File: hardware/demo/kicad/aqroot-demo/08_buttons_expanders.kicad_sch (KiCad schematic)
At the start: 34 parts, among them SW2 UP, SW3 DOWN, SW4 LEFT, SW5 RIGHT, SW6 A_SELECT, SW7 B_BACK, U2 PCAL9535APW, U23 PCAL9535APW, U3 PCAL9535APW

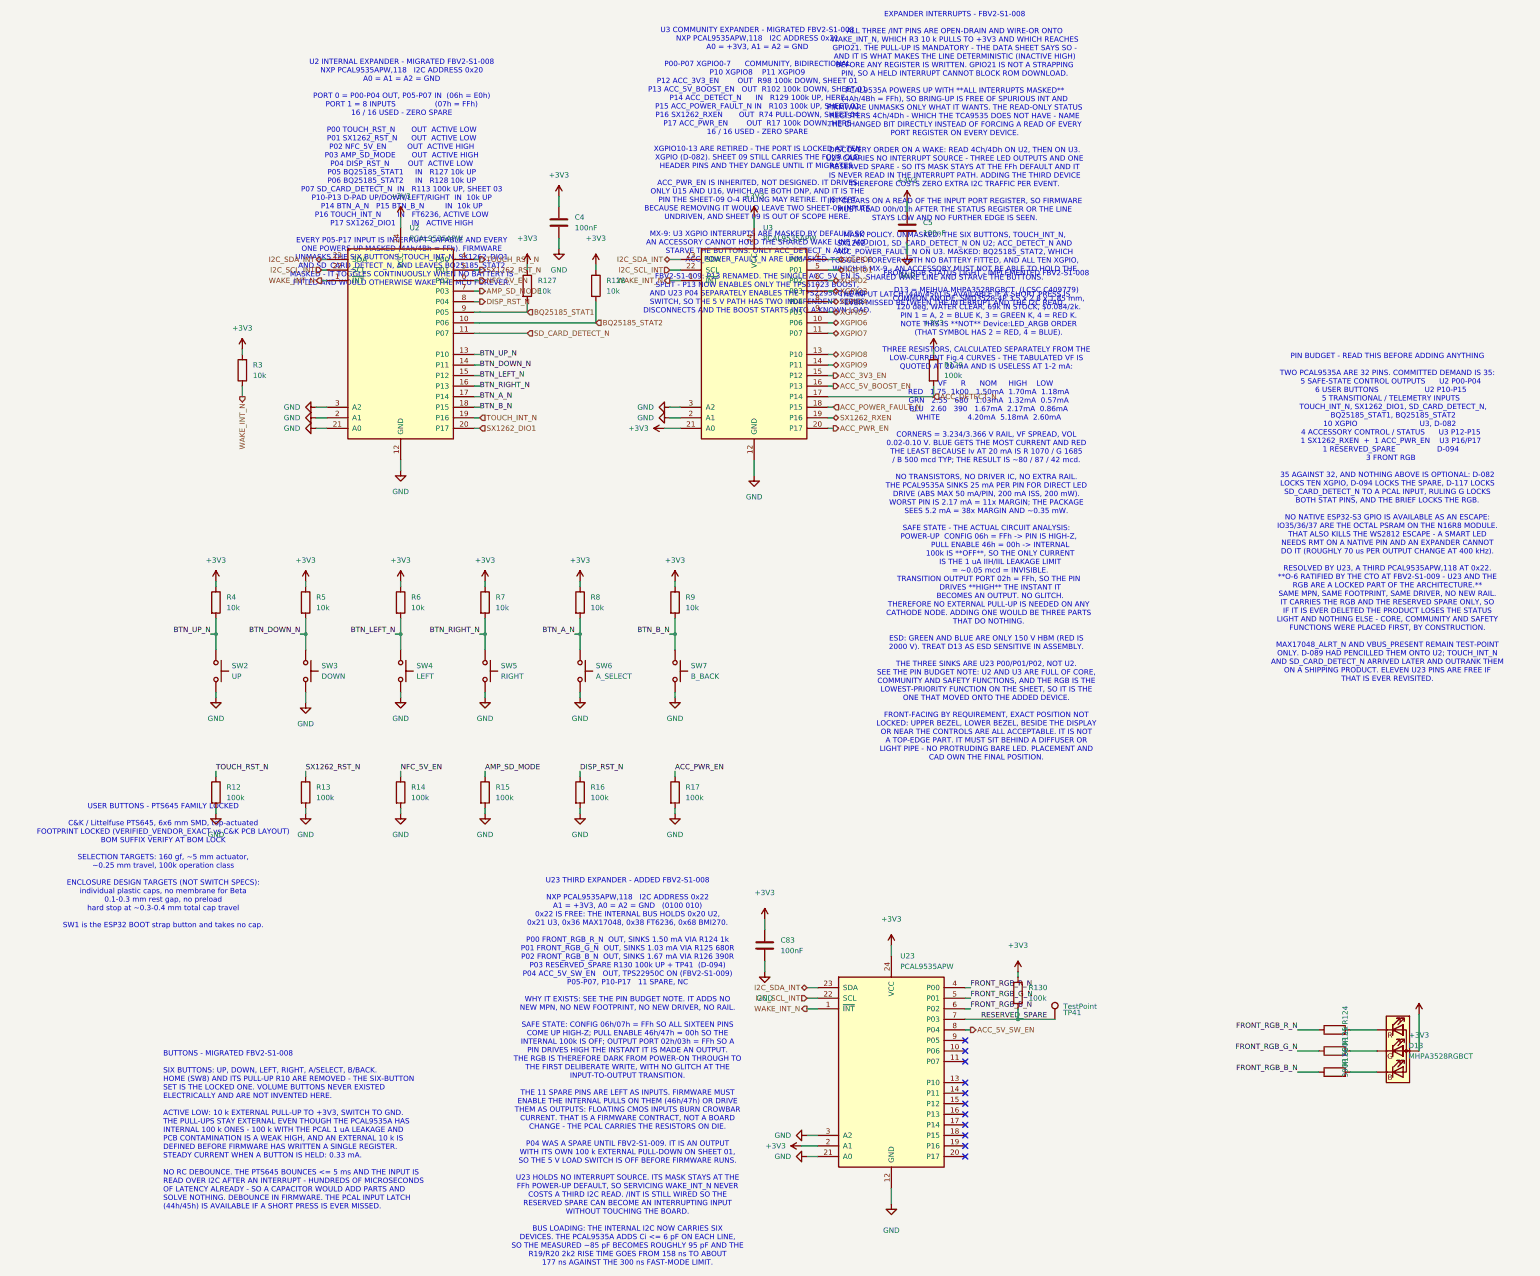
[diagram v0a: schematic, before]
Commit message: demo: apply schematic simplification ECO
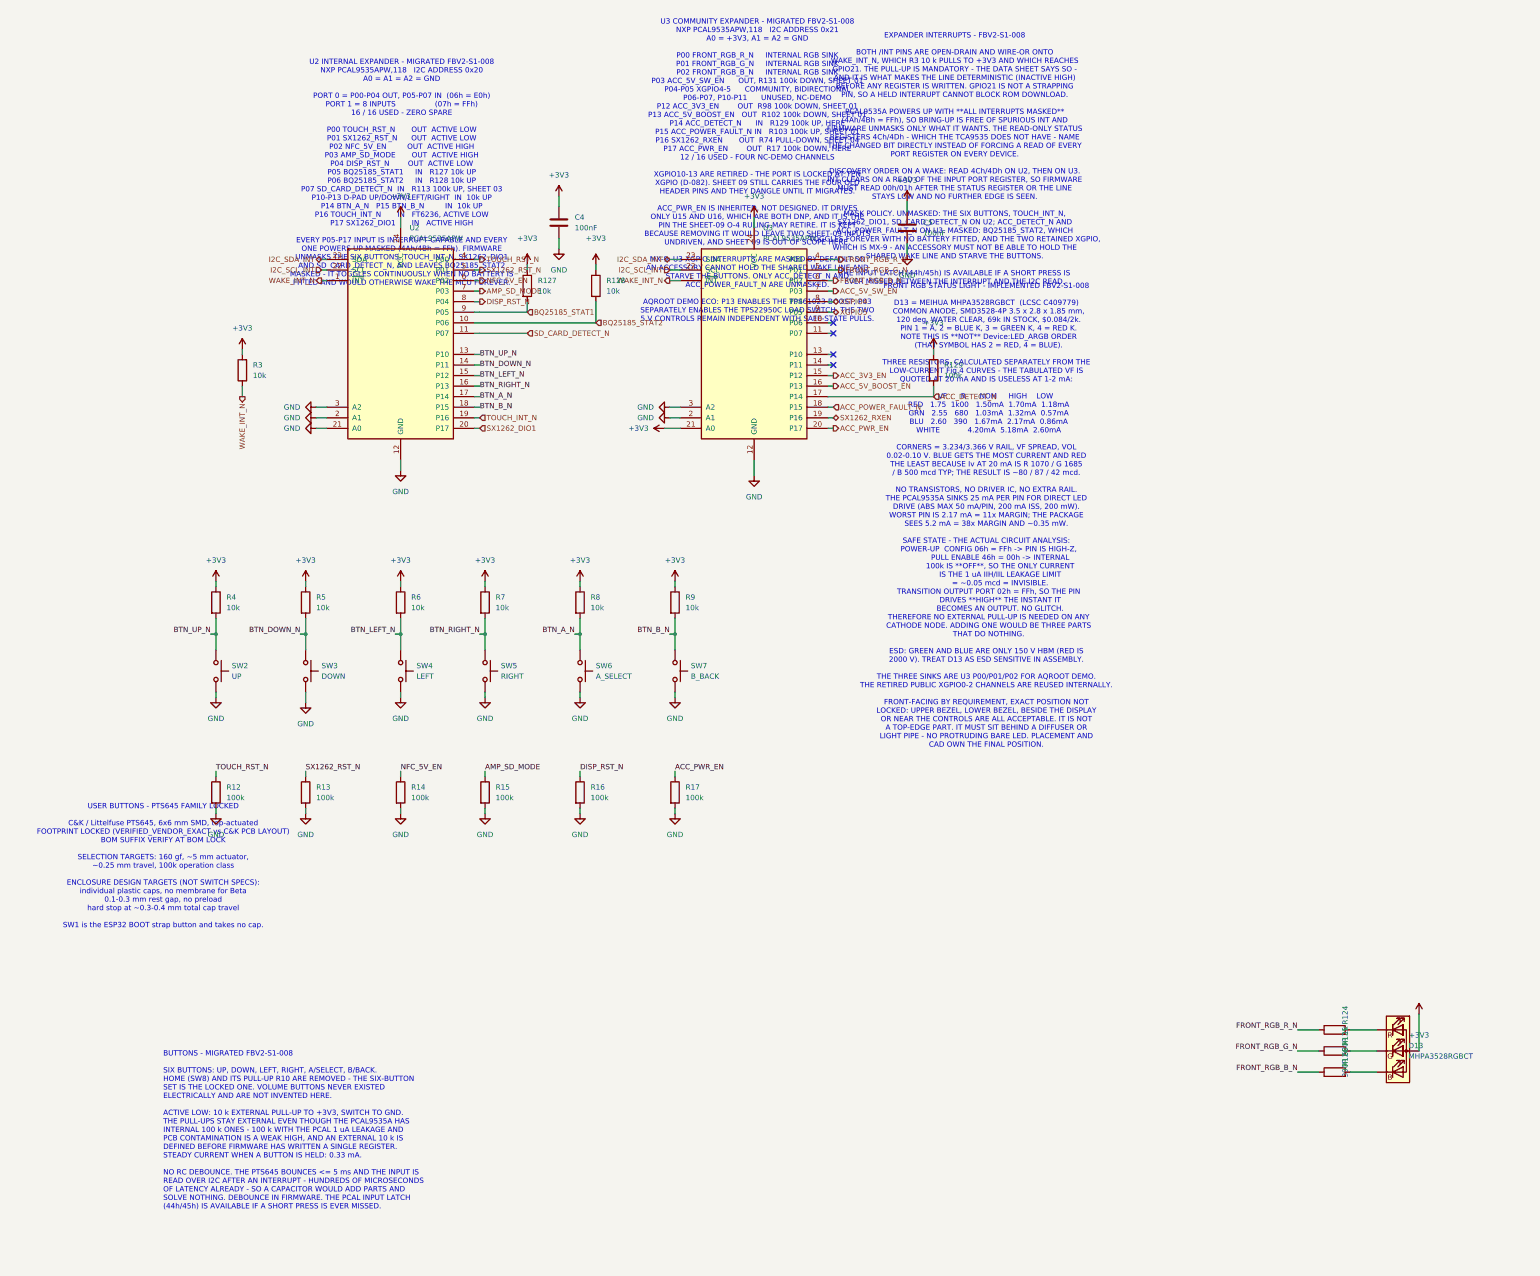
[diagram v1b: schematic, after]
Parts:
- removed C83: 100nF, Capacitor_SMD:C_0603_1608Metric, symbol Device:C
- removed R130: 100k, Resistor_SMD:R_0603_1608Metric, symbol Device:R
- removed TP41: TestPoint, TestPoint:TestPoint_Pad_D1.0mm, symbol Connector:TestPoint
- removed U23: PCAL9535APW, Package_SO:TSSOP-24_4.4x7.8mm_P0.65mm, symbol AQROOT_Beta:PCAL9535APW
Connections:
- net XGPIO0 is gone; now on net FRONT_RGB_R_N: U3.4 (P00)
- net XGPIO1 is gone; now on net FRONT_RGB_G_N: U3.5 (P01)
- net XGPIO2 is gone; now on net FRONT_RGB_B_N: U3.6 (P02)
- net XGPIO3 is gone; now on net ACC_5V_SW_EN: U3.7 (P03)
- net XGPIO6: no longer names the net of U3.10 (P06)
- net XGPIO7: no longer names the net of U3.11 (P07)
- net XGPIO8: no longer names the net of U3.13 (P10)
- net XGPIO9: no longer names the net of U3.14 (P11)
- no-connect marks 11 -> 4
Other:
- note added: "EXPANDER INTERRUPTS - FBV2-S1-008 BOTH /INT PINS ARE OPEN-DRAIN AND WIRE-OR ONTO WAKE_INT_N, WHICH R3 10 k PULLS TO +3V3 AND WHICH REACHES GPIO21. THE PULL-UP IS MANDATORY - THE DATA SHEET SAYS SO - AND IT IS WHAT MAKES THE LINE DETERMINISTIC (INACTIVE HIGH) BEFORE ANY REGISTER IS WRITTEN. GPIO21 IS NOT A STRAPPING PIN, SO A HELD INTERRUPT CANNOT BLOCK ROM DOWNLOAD. PCAL9535A POWERS UP WITH **ALL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"
- note added: "U3 COMMUNITY EXPANDER - MIGRATED FBV2-S1-008 NXP PCAL9535APW,118 I2C ADDRESS 0x21 A0 = +3V3, A1 = A2 = GND P00 FRONT_RGB_R_N INTERNAL RGB SINK P01 FRONT_RGB_G_N INTERNAL RGB SINK P02 FRONT_RGB_B_N INTERNAL RGB SINK P03 ACC_5V_SW_EN OUT, R131 100k DOWN, SHEET 01 P04-P05 XGPIO4-5 COMMUNITY, BIDIRECTIONAL P06-P07, P10-P11 UNUSED, NC-DEMO P12 ACC_3V3_EN OUT R98 100k DOWN, SHEET 01 P13 ACC_5V_BOOST_EN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"
- note removed: "EXPANDER INTERRUPTS - FBV2-S1-008 ALL THREE /INT PINS ARE OPEN-DRAIN AND WIRE-OR ONTO WAKE_INT_N, WHICH R3 10 k PULLS TO +3V3 AND WHICH REACHES GPIO21. THE PULL-UP IS MANDATORY - THE DATA SHEET SAYS SO - AND IT IS WHAT MAKES THE LINE DETERMINISTIC (INACTIVE HIGH) BEFORE ANY REGISTER IS WRITTEN. GPIO21 IS NOT A STRAPPING PIN, SO A HELD INTERRUPT CANNOT BLOCK ROM DOWNLOAD. PCAL9535A POWERS UP WITH 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"
- note removed: "PIN BUDGET - READ THIS BEFORE ADDING ANYTHING TWO PCAL9535A ARE 32 PINS. COMMITTED DEMAND IS 35: 5 SAFE-STATE CONTROL OUTPUTS U2 P00-P04 6 USER BUTTONS U2 P10-P15 5 TRANSITIONAL / TELEMETRY INPUTS TOUCH_INT_N, SX1262_DIO1, SD_CARD_DETECT_N, BQ25185_STAT1, BQ25185_STAT2 10 XGPIO U3, D-082 4 ACCESSORY CONTROL / STATUS U3 P12-P15 1 SX1262_RXEN + 1 ACC_PWR_EN U3 P16/P17 1 RESERVED_SPARE D-094 3 FRONT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"
- note removed: "U23 THIRD EXPANDER - ADDED FBV2-S1-008 NXP PCAL9535APW,118 I2C ADDRESS 0x22 A1 = +3V3, A0 = A2 = GND (0100 010) 0x22 IS FREE: THE INTERNAL BUS HOLDS 0x20 U2, 0x21 U3, 0x36 MAX17048, 0x38 FT6236, 0x68 BMI270. P00 FRONT_RGB_R_N OUT, SINKS 1.50 mA VIA R124 1k P01 FRONT_RGB_G_N OUT, SINKS 1.03 mA VIA R125 680R P02 FRONT_RGB_B_N OUT, SINKS 1.67 mA VIA R126 390R P03 RESERVED_SPARE R130 100k UP + TP41 (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"
- note removed: "U3 COMMUNITY EXPANDER - MIGRATED FBV2-S1-008 NXP PCAL9535APW,118 I2C ADDRESS 0x21 A0 = +3V3, A1 = A2 = GND P00-P07 XGPIO0-7 COMMUNITY, BIDIRECTIONAL P10 XGPIO8 P11 XGPIO9 P12 ACC_3V3_EN OUT R98 100k DOWN, SHEET 01 P13 ACC_5V_BOOST_EN OUT R102 100k DOWN, SHEET 01 P14 ACC_DETECT_N IN R129 100k UP, HERE P15 ACC_POWER_FAULT_N IN R103 100k UP, SHEET 01 P16 SX1262_RXEN OUT R74 PULL-DOWN, SHEET 04 P17 A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"
